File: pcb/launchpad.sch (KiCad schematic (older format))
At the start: 29 parts, among them J1 TYPE-C-31-M-12, J2 ICSP, SW0 CherryMX, SW1 CherryMX, SW2 CherryMX, SW3 CherryMX, SW4 CherryMX, SW5 CherryMX, SW6 CherryMX, U1 ATmega32U4-MUR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

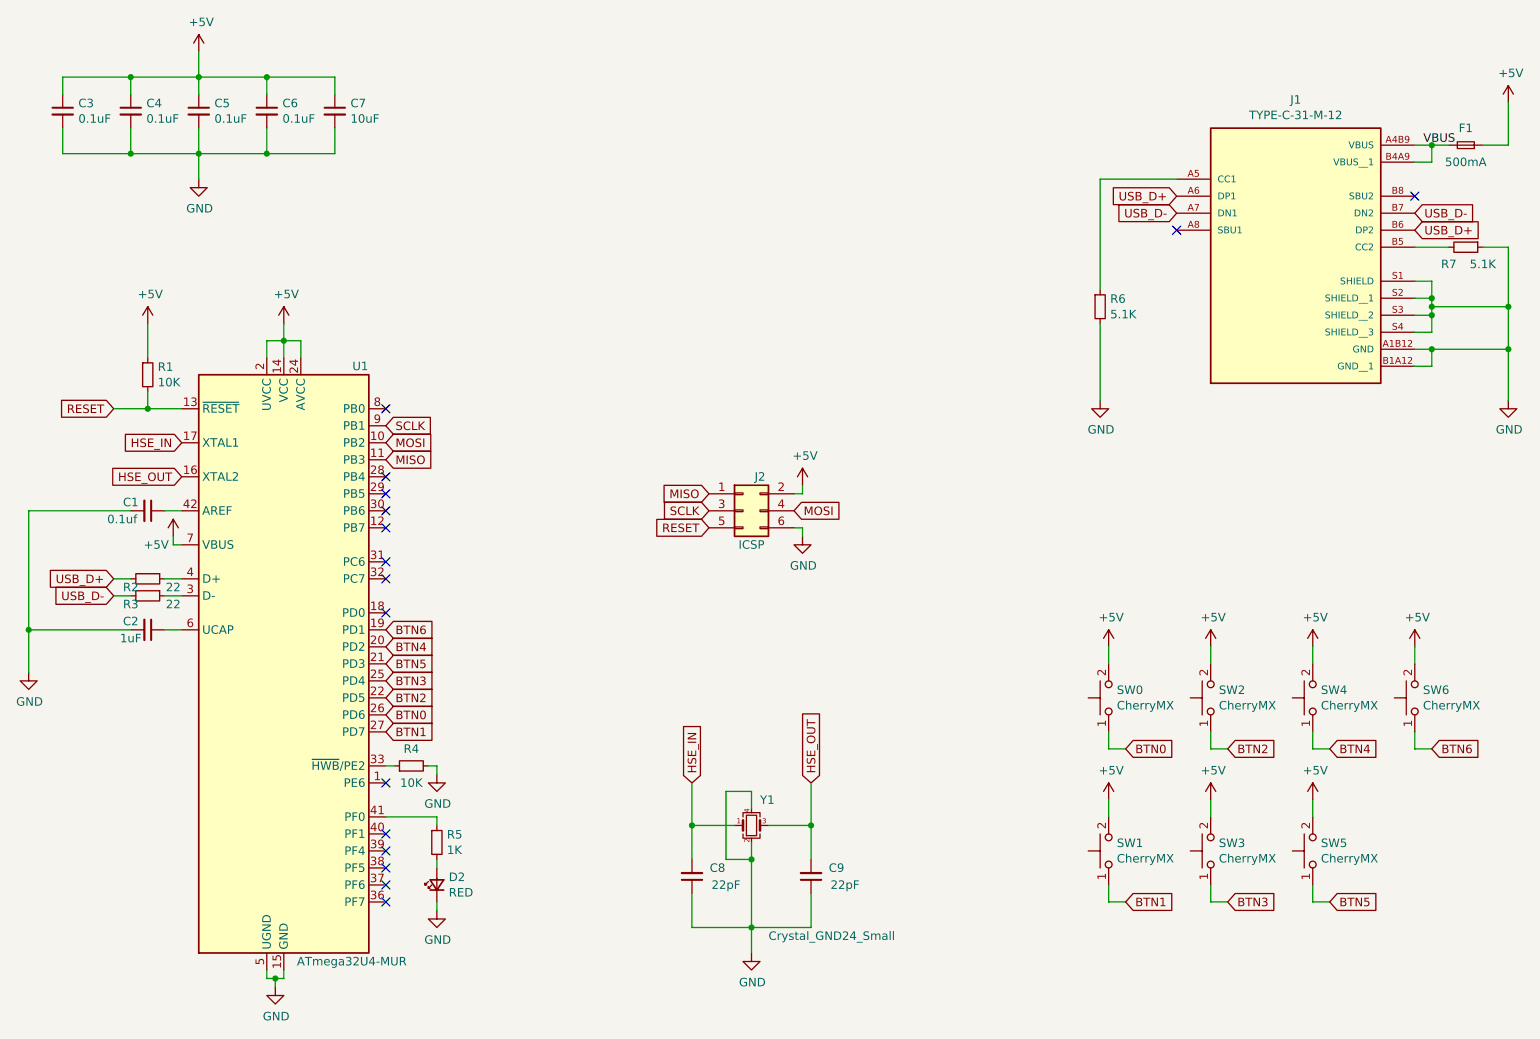
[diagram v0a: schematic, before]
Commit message: So made the buttons active low. And found that I used the wrong ICSP header
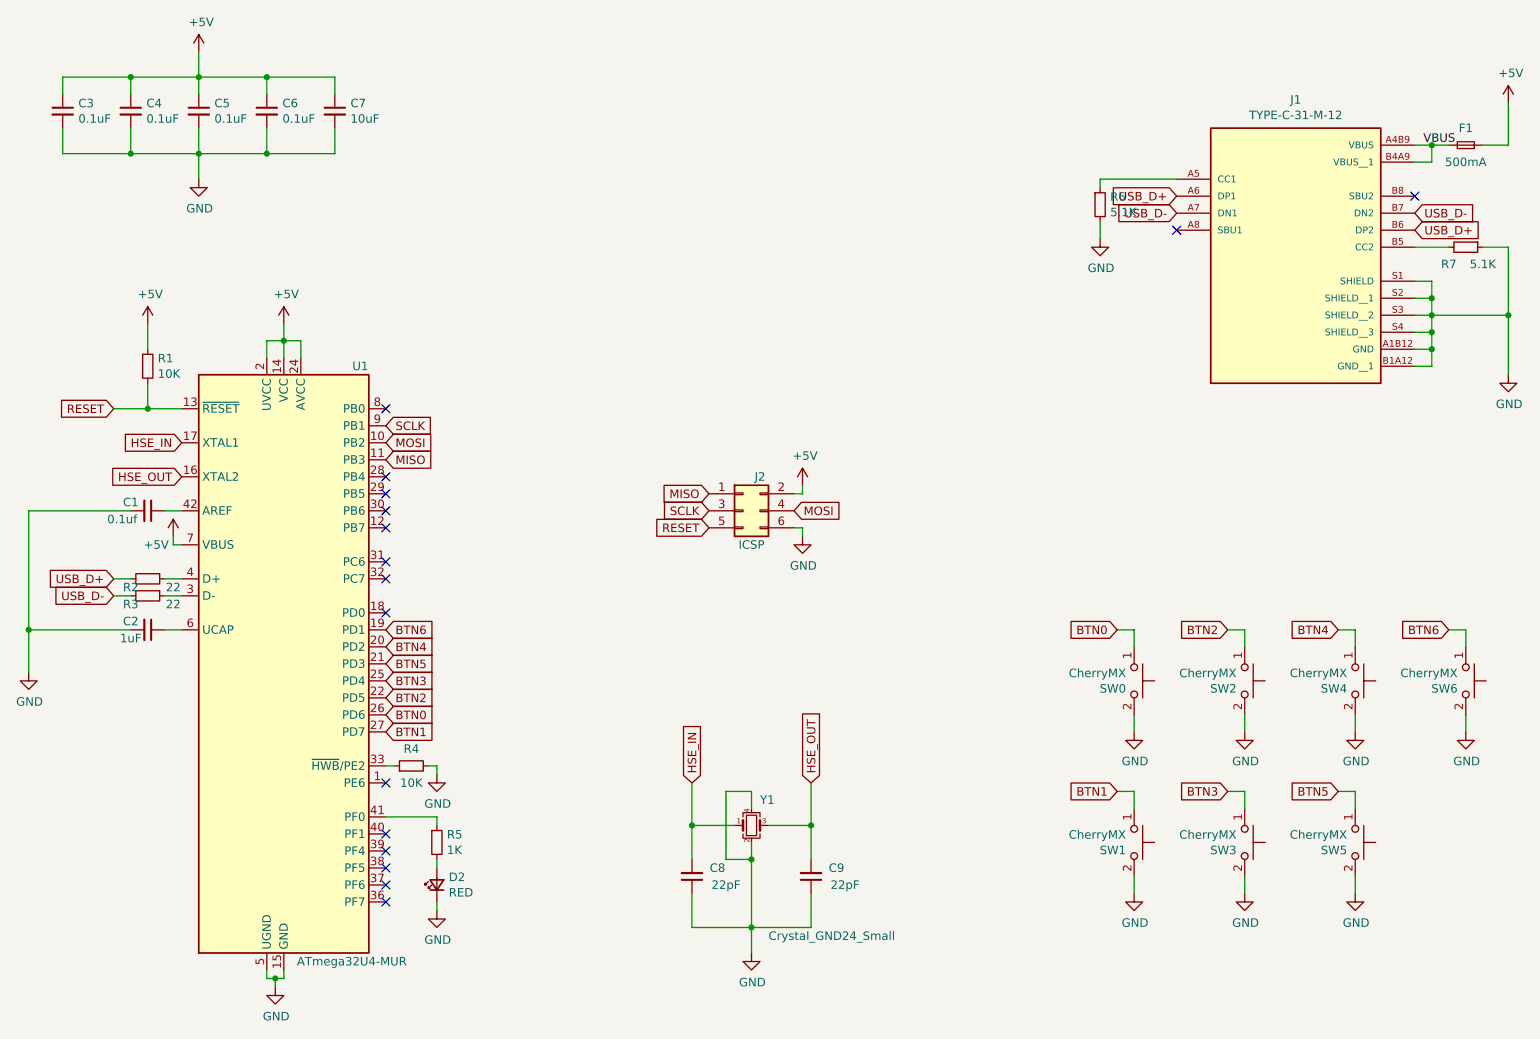
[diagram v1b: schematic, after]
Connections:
- net +5V: no longer SW0.2, SW1.2, SW2.2, SW3.2, SW4.2, SW5.2, SW6.2
- net GND: now also SW0.2, SW1.2, SW2.2, SW3.2, SW4.2, SW5.2, SW6.2
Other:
- moved on the sheet: R1, R6, SW0, SW1, SW2, SW3, SW4, SW5, SW6

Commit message: Updated pinheader to appropiate size
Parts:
- J2: footprint Connector_PinHeader_1.00mm:PinHeader_2x03_P1.00mm_Vertical -> Connector_PinHeader_2.54mm:PinHeader_2x03_P2.54mm_Vertical
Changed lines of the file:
@@
 F 0 "J2" H 5550 4100 50  0000 C CNN
 F 1 "ICSP" H 5500 3700 50  0000 C CNN
-F 2 "Connector_PinHeader_1.00mm:PinHeader_2x03_P1.00mm_Vertical" H 5450 3900 50  0001 C CNN
+F 2 "Connector_PinHeader_2.54mm:PinHeader_2x03_P2.54mm_Vertical" H 5450 3900 50  0001 C CNN
 F 3 "~" H 5450 3900 50  0001 C CNN
 	1    5450 3900

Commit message: Order is completed
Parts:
- C1: value 0.1uf -> 0.1uF
- C7: LCSC C1634 -> C19702
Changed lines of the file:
@@
 F 2 "Capacitor_SMD:C_0603_1608Metric" H 3050 1550 50  0001 C CNN
 F 3 "~" H 3050 1550 50  0001 C CNN
-F 4 "C1634" H 3050 1550 50  0001 C CNN "LCSC"
+F 4 "C19702 " H 3050 1550 50  0001 C CNN "LCSC"
 	1    3050 1550
 	1    0    0    -1
@@
 P 1950 3900
 F 0 "C1" V 1900 3800 50  0000 C CNN
-F 1 "0.1uf" V 2000 3750 50  0000 C CNN
+F 1 "0.1uF" V 2000 3750 50  0000 C CNN
 F 2 "Capacitor_SMD:C_0603_1608Metric" H 1950 3900 50  0001 C CNN
 F 3 "~" H 1950 3900 50  0001 C CNN
